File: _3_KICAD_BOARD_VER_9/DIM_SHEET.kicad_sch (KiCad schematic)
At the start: 25 parts, among them J1 HTEC8-160-01-X-DV-A-BL-X

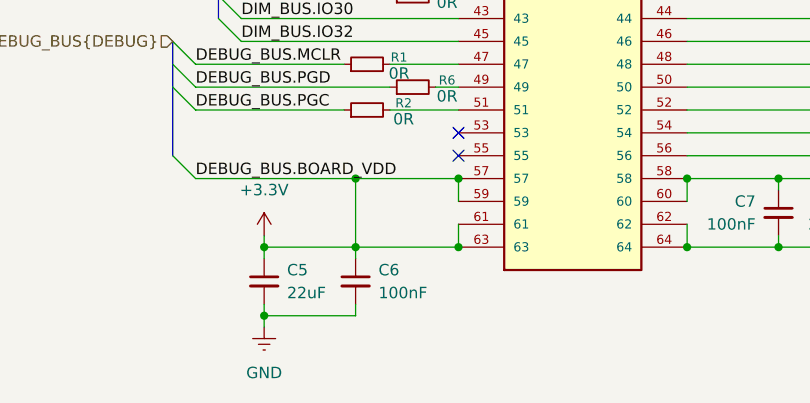
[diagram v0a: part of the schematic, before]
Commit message: feat : vdd, gnd, vin routing done
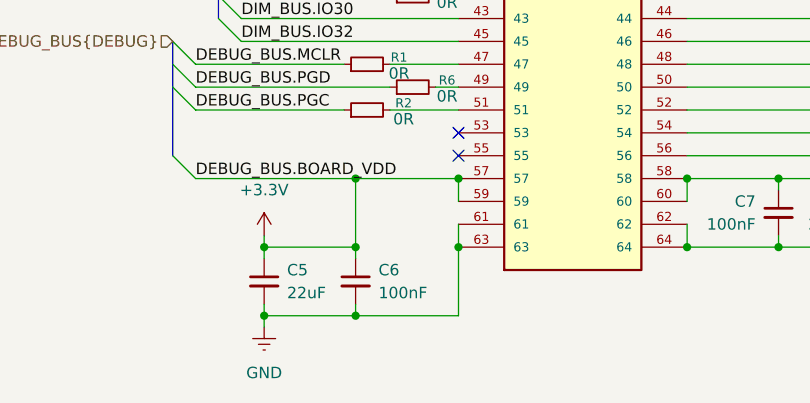
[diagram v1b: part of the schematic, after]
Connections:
- net +3.3V: no longer J1.61, J1.63
- net GND: now also J1.61, J1.63
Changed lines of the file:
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@@
+	)
+	(junction
+		(at 67.31 128.27)
+		(diameter 0)
+		(color 0 0 0 0)
 	)
 	(junction
@@
 	)
 	(junction
-		(at 78.74 120.65)
-		(diameter 0)
-		(color 0 0 0 0)
-	)
-	(junction
 		(at 57.15 128.27)
 		(diameter 0)
@@
 	)
 	(junction
+		(at 78.74 120.65)
+		(diameter 0)
+		(color 0 0 0 0)
+	)
+	(junction
 		(at 219.71 105.41)
 		(diameter 0)
@@
 		)
 	)
+	(wire
+		(pts
+			(xy 78.74 128.27) (xy 67.31 128.27)
+		)
+		(stroke
+			(width 0)
+			(type default)
+		)
+	)
 	(bus
 		(pts
@@
 		)
 	)
-	(wire
-		(pts
-			(xy 67.31 120.65) (xy 78.74 120.65)
-		)
-		(stroke
-			(width 0)
-			(type default)
-		)
-	)
 	(bus
 		(pts
@@
 		)
 		(stroke
+			(width 0)
+			(type default)
+		)
+	)
+	(wire
+		(pts
+			(xy 78.74 120.65) (xy 78.74 128.27)
+		)
+		(stroke
